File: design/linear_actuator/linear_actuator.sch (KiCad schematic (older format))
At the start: 28 parts, among them J1 Conn_01x02, J2 Conn_01x05, J3 Conn_01x05, Q1 BC337, Q2 BC337, Q3 BC337, Q4 BC337, Q5 Q_PMOS_GDS, Q6 Q_NMOS_GDS, Q7 Q_PMOS_GDS, Q8 Q_NMOS_GDS, U1 DAC5571, U2 DAC5571, U3 TS391ILT, U4 TS391ILT, U5 R-78-0.5

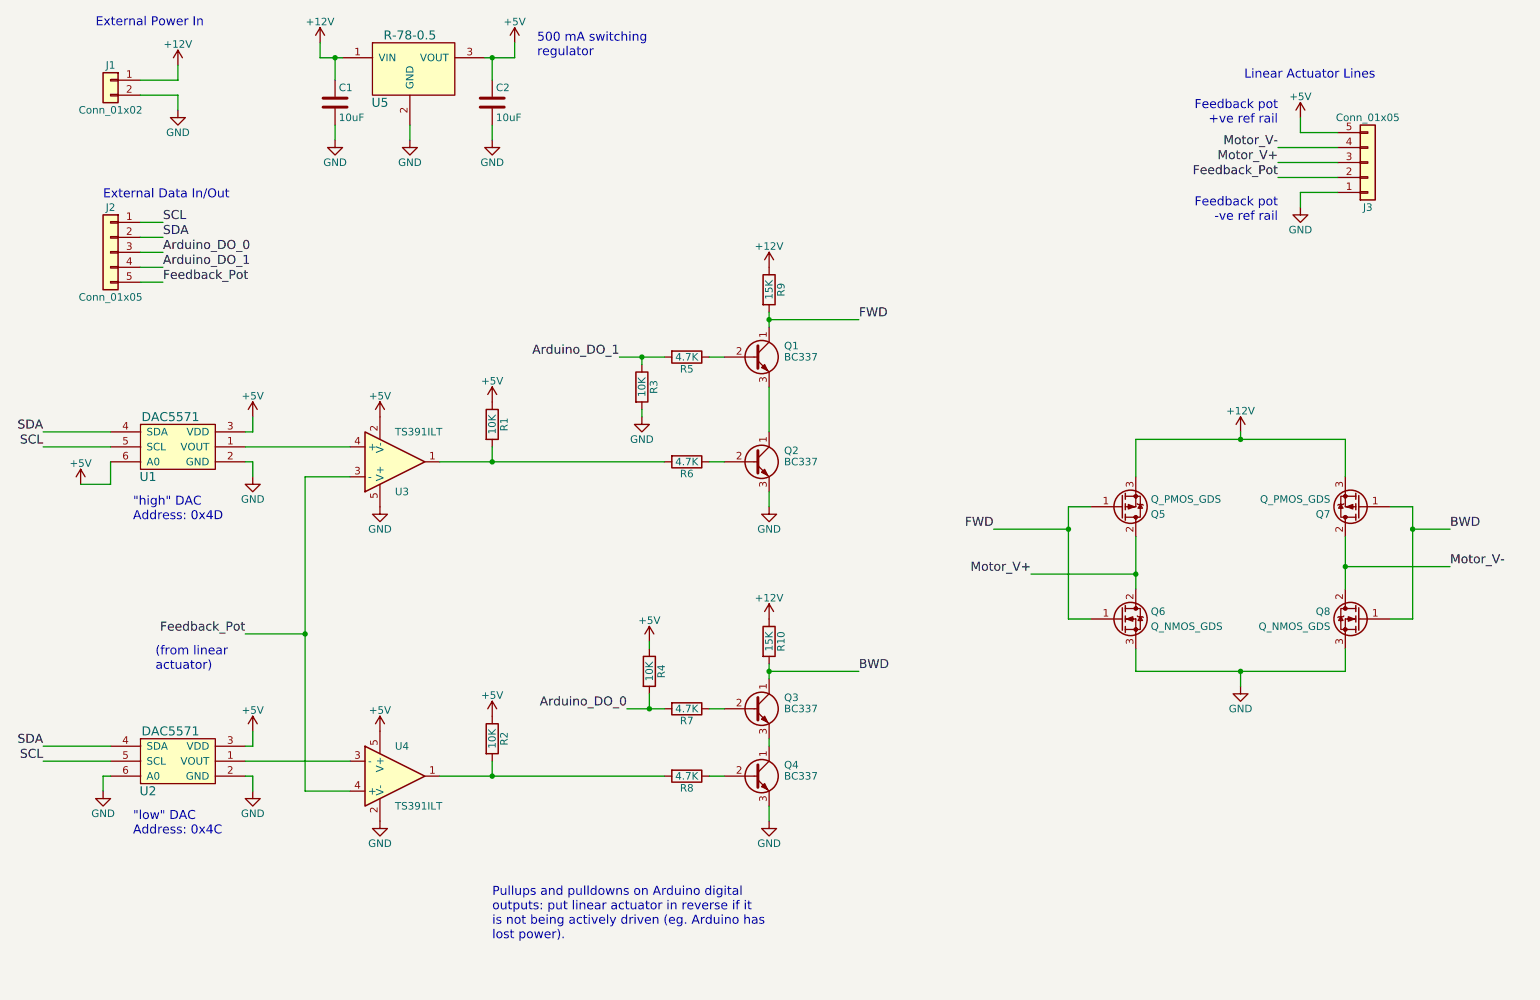
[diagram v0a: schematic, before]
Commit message: Specify part numbers for the H bridge MOSFETS
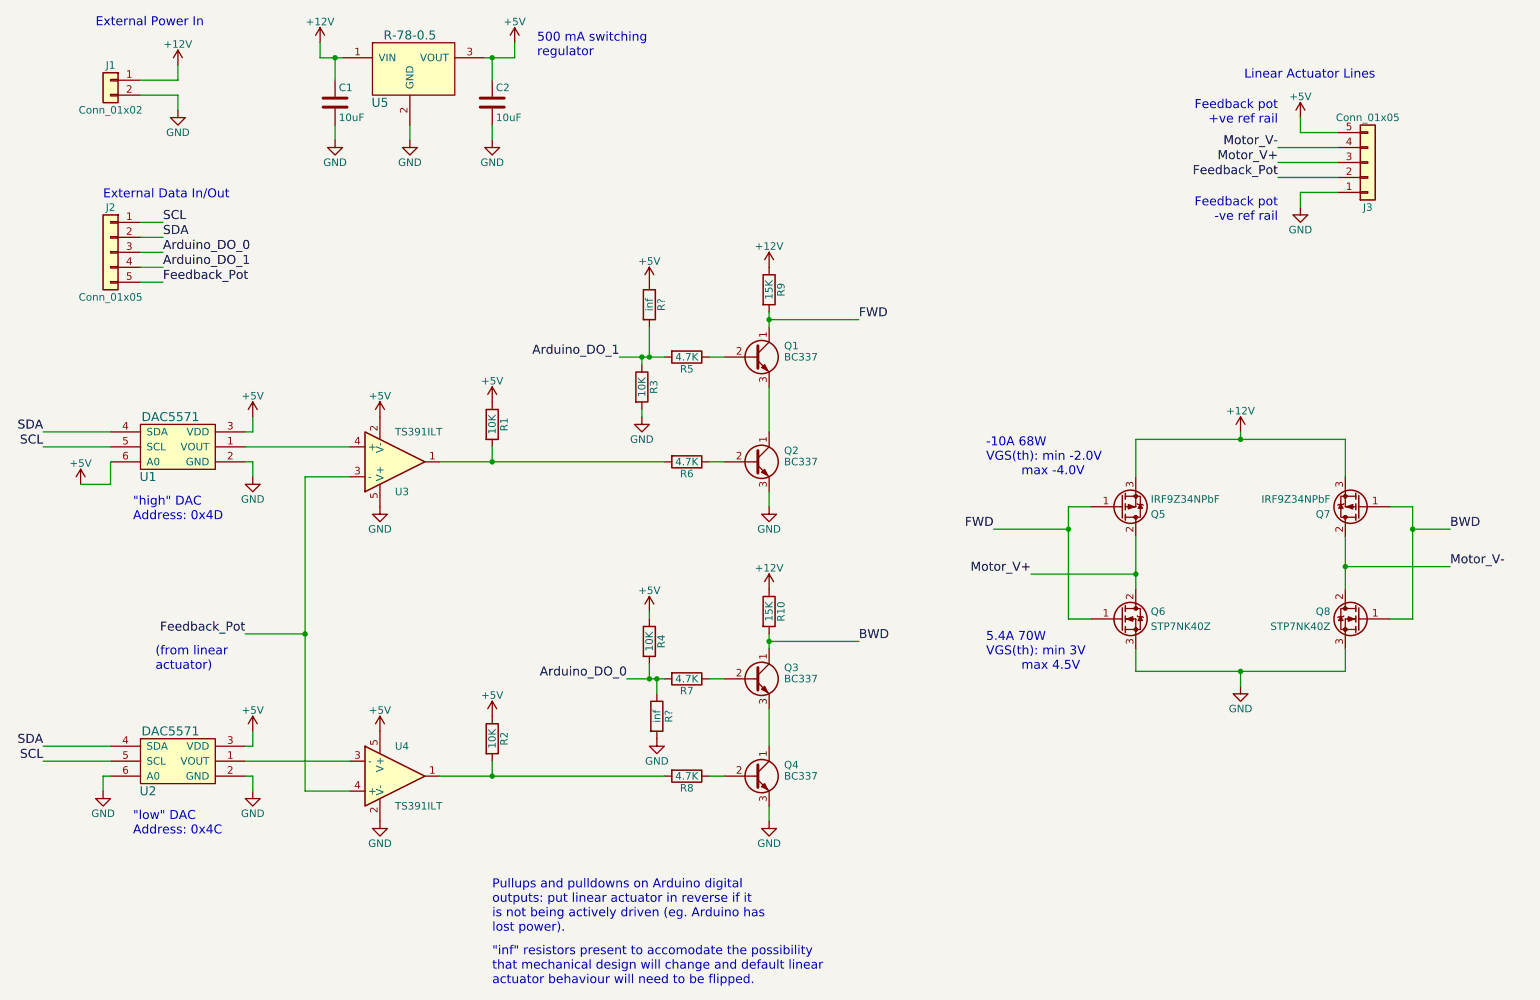
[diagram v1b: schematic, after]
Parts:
- added R? (x2): inf, symbol R
- Q5, Q7: value Q_PMOS_GDS -> IRF9Z34NPbF
- Q6, Q8: value Q_NMOS_GDS -> STP7NK40Z
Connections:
- net +5V: now also R?.1
- net Arduino_DO_0: now also R?.1
- net Arduino_DO_1: now also R?.2
- net GND: now also R?.2
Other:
- note added: ""inf" resistors present to accomodate the possibility\nthat mechanical design will change and default linear\nactuator behaviour will need to be flipped."
- note added: "-10A 68W\nVGS(th): min -2.0V\n max -4.0V"
- note added: "5.4A 70W\nVGS(th): min 3V\n max 4.5V"
- moved on the sheet: Q3, R10, R4, R7
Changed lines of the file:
@@
 L BC337 Q3
 U 1 1 5A95D0CE
-P 5800 5800
-F 0 "Q3" H 6000 5875 50  0000 L CNN
-F 1 "BC337" H 6000 5800 50  0000 L CNN
-F 2 "TO_SOT_Packages_THT:TO-92_Molded_Narrow" H 6000 5725 50  0001 L CIN
-F 3 "" H 5800 5800 50  0001 L CNN
-	1    5800 5800
+P 5800 5600
+F 0 "Q3" H 6000 5675 50  0000 L CNN
+F 1 "BC337" H 6000 5600 50  0000 L CNN
+F 2 "TO_SOT_Packages_THT:TO-92_Molded_Narrow" H 6000 5525 50  0001 L CIN
+F 3 "" H 5800 5600 50  0001 L CNN
+	1    5800 5600
 	1    0    0    -1
 $EndComp
@@
 L R R7
 U 1 1 5A95DF39
-P 5350 5800
-F 0 "R7" V 5430 5800 50  0000 C CNN
-F 1 "4.7K" V 5350 5800 50  0000 C CNN
-F 2 "" V 5280 5800 50  0001 C CNN
-F 3 "" H 5350 5800 50  0001 C CNN
-	1    5350 5800
+P 5350 5600
+F 0 "R7" V 5430 5600 50  0000 C CNN
+F 1 "4.7K" V 5350 5600 50  0000 C CNN
+F 2 "" V 5280 5600 50  0001 C CNN
+F 3 "" H 5350 5600 50  0001 C CNN
+	1    5350 5600
 	0    1    1    0
 $EndComp
@@
 Text Label 4900 3450 2    60   ~ 0
 Arduino_DO_1
-Text Label 4950 5800 2    60   ~ 0
+Text Label 4950 5600 2    60   ~ 0
 Arduino_DO_0
 $Comp
@@
 P 8250 4450
 F 0 "Q5" H 8450 4500 50  0000 L CNN
-F 1 "Q_PMOS_GDS" H 8450 4400 50  0000 L CNN
+F 1 "IRF9Z34NPbF" H 8450 4400 50  0000 L CNN
 F 2 "" H 8450 4550 50  0001 C CNN
 F 3 "" H 8250 4450 50  0001 C CNN
@@
 P 9850 4450
 F 0 "Q7" H 10050 4500 50  0000 L CNN
-F 1 "Q_PMOS_GDS" H 10050 4400 50  0000 L CNN
+F 1 "IRF9Z34NPbF" H 10050 4400 50  0000 L CNN
 F 2 "" H 10050 4550 50  0001 C CNN
 F 3 "" H 9850 4450 50  0001 C CNN
@@
 P 8250 5200
 F 0 "Q6" H 8450 5250 50  0000 L CNN
-F 1 "Q_NMOS_GDS" H 8450 5150 50  0000 L CNN
+F 1 "STP7NK40Z" H 8450 5150 50  0000 L CNN
 F 2 "" H 8450 5300 50  0001 C CNN
 F 3 "" H 8250 5200 50  0001 C CNN
@@
 P 9850 5200
 F 0 "Q8" H 10050 5250 50  0000 L CNN
-F 1 "Q_NMOS_GDS" H 10050 5150 50  0000 L CNN
+F 1 "STP7NK40Z" H 10050 5150 50  0000 L CNN
 F 2 "" H 10050 5300 50  0001 C CNN
 F 3 "" H 9850 5200 50  0001 C CNN
@@
 L R R10
 U 1 1 5A96393E
-P 5900 5350
-F 0 "R10" V 5980 5350 50  0000 C CNN
-F 1 "15K" V 5900 5350 50  0000 C CNN
-F 2 "" V 5830 5350 50  0001 C CNN
-F 3 "" H 5900 5350 50  0001 C CNN
-	1    5900 5350
+P 5900 5150
+F 0 "R10" V 5980 5150 50  0000 C CNN
+F 1 "15K" V 5900 5150 50  0000 C CNN
+F 2 "" V 5830 5150 50  0001 C CNN
+F 3 "" H 5900 5150 50  0001 C CNN
+	1    5900 5150
 	1    0    0    -1
 $EndComp
@@
 Text Label 6500 3200 0    60   ~ 0
 FWD
-Text Label 6500 5550 0    60   ~ 0
+Text Label 6500 5350 0    60   ~ 0
 BWD
 Text Label 7400 4600 2    60   ~ 0
@@
 L R R4
 U 1 1 5A96BB5C
-P 5100 5550
-F 0 "R4" V 5180 5550 50  0000 C CNN
-F 1 "10K" V 5100 5550 50  0000 C CNN
-F 2 "" V 5030 5550 50  0001 C CNN
-F 3 "" H 5100 5550 50  0001 C CNN
-	1    5100 5550
+P 5100 5350
+F 0 "R4" V 5180 5350 50  0000 C CNN
+F 1 "10K" V 5100 5350 50  0000 C CNN
+F 2 "" V 5030 5350 50  0001 C CNN
+F 3 "" H 5100 5350 50  0001 C CNN
+	1    5100 5350
 	1    0    0    -1
 $EndComp
@@
 L +5V #PWR21
 U 1 1 5A96CA86
-P 5100 5350
-F 0 "#PWR21" H 5100 5200 50  0001 C CNN
-F 1 "+5V" H 5100 5490 50  0000 C CNN
-F 2 "" H 5100 5350 50  0001 C CNN
-F 3 "" H 5100 5350 50  0001 C CNN
-	1    5100 5350
+P 5100 5150
+F 0 "#PWR21" H 5100 5000 50  0001 C CNN
+F 1 "+5V" H 5100 5290 50  0000 C CNN
+F 2 "" H 5100 5150 50  0001 C CNN
+F 3 "" H 5100 5150 50  0001 C CNN
+	1    5100 5150
 	1    0    0    -1
 $EndComp
@@
 	1    0    0    -1
 $EndComp
-Text Notes 4050 7350 0    60   ~ 0
+Text Notes 4050 7300 0    60   ~ 0
 Pullups and pulldowns on Arduino digital\noutputs: put linear actuator in reverse if it\nis not being actively driven (eg. Arduino has\nlost power).
 Text Notes 1800 5550 0    60   ~ 0
@@
 L +12V #PWR?
 U 1 1 5A973E8F
-P 5900 5200
-F 0 "#PWR?" H 5900 5050 50  0001 C CNN
-F 1 "+12V" H 5900 5340 50  0000 C CNN
-F 2 "" H 5900 5200 50  0001 C CNN
-F 3 "" H 5900 5200 50  0001 C CNN
-	1    5900 5200
+P 5900 5000
+F 0 "#PWR?" H 5900 4850 50  0001 C CNN
+F 1 "+12V" H 5900 5140 50  0000 C CNN
+F 2 "" H 5900 5000 50  0001 C CNN
+F 3 "" H 5900 5000 50  0001 C CNN
+	1    5900 5000
 	1    0    0    -1
 $EndComp
@@
 	4050 6250 4050 6150
 Wire Wire Line
-	5900 6000 5900 6050
+	5900 5800 5900 6050
 Wire Wire Line
 	5900 3150 5900 3250
@@
 	5900 6450 5900 6550
 Wire Wire Line
-	5500 5800 5600 5800
+	5500 5600 5600 5600
 Wire Wire Line
 	5500 6250 5600 6250
@@
 Connection ~ 8350 4900
 Wire Wire Line
-	4950 5800 5200 5800
-Wire Wire Line
-	5100 5350 5100 5400
-Wire Wire Line
-	5100 5700 5100 5800
-Connection ~ 5100 5800
+	4950 5600 5200 5600
+Wire Wire Line
+	5100 5150 5100 5200
+Wire Wire Line
+	5100 5500 5100 5600
+Connection ~ 5100 5600
 Wire Wire Line
 	5050 3850 5050 3800
@@
 	10200 4450 10200 5200
 Wire Wire Line
-	5900 5500 5900 5600
-Wire Wire Line
-	6500 5550 5900 5550
-Connection ~ 5900 5550
+	5900 5300 5900 5400
+Wire Wire Line
+	6500 5350 5900 5350
+Connection ~ 5900 5350
 Wire Wire Line
 	6500 3200 5900 3200
@@
 	2800 4250 2800 6350
 Connection ~ 2800 5300
+$Comp
+L R R?
+U 1 1 5A9C57FF
+P 5100 3100
+F 0 "R?" V 5180 3100 50  0000 C CNN
+F 1 "inf" V 5100 3100 50  0000 C CNN
+F 2 "" V 5030 3100 50  0001 C CNN
+F 3 "" H 5100 3100 50  0001 C CNN
+	1    5100 3100
+	1    0    0    -1
+$EndComp
+$Comp
+L +5V #PWR?
+U 1 1 5A9C5C6D
+P 5100 2950
+F 0 "#PWR?" H 5100 2800 50  0001 C CNN
+F 1 "+5V" H 5100 3090 50  0000 C CNN
+F 2 "" H 5100 2950 50  0001 C CNN
+F 3 "" H 5100 2950 50  0001 C CNN
+	1    5100 2950
+	1    0    0    -1
+$EndComp
+Wire Wire Line
+	5100 3250 5100 3450
+Connection ~ 5100 3450
+$Comp
+L R R?
+U 1 1 5A9C61DB
+P 5150 5850
+F 0 "R?" V 5230 5850 50  0000 C CNN
+F 1 "inf" V 5150 5850 50  0000 C CNN
+F 2 "" V 5080 5850 50  0001 C CNN
+F 3 "" H 5150 5850 50  0001 C CNN
+	1    5150 5850
+	1    0    0    -1
+$EndComp
+$Comp
+L GND #PWR?
+U 1 1 5A9C6395
+P 5150 6000
+F 0 "#PWR?" H 5150 5750 50  0001 C CNN
+F 1 "GND" H 5150 5850 50  0000 C CNN
+F 2 "" H 5150 6000 50  0001 C CNN
+F 3 "" H 5150 6000 50  0001 C CNN
+	1    5150 6000
+	1    0    0    -1
+$EndComp
+Wire Wire Line
+	5150 5700 5150 5600
+Connection ~ 5150 5600
+Text Notes 4050 7650 0    60   ~ 0
+"inf" resistors present to accomodate the possibility\nthat mechanical design will change and default linear\nactuator behaviour will need to be flipped.
+Text Notes 7350 5550 0    60   ~ 0
+5.4A 70W\nVGS(th): min 3V\n         max 4.5V
+Text Notes 7350 4250 0    60   ~ 0
+-10A 68W\nVGS(th): min -2.0V\n         max -4.0V
 $EndSCHEMATC
